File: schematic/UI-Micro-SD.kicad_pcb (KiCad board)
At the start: 2 copper layers, 86.4 x 51.4 mm, 30 parts, among them IC1 TCA9534PWR, J1 47309-3351, J2 Conn_02x04_Odd_Even, J3 Conn_02x05_Odd_Even, J4 Conn_02x03_Odd_Even, J5 Conn_02x08_Odd_Even, J6 Conn_01x08, J7 Conn_02x08_Odd_Even, J8 Solder-Jumper-3-3-3-Open, Q1 BSS138, U1 SFV14R-2STE1HLF, U2 DizzyBITLogo, U3 DizzyBIT-Layout

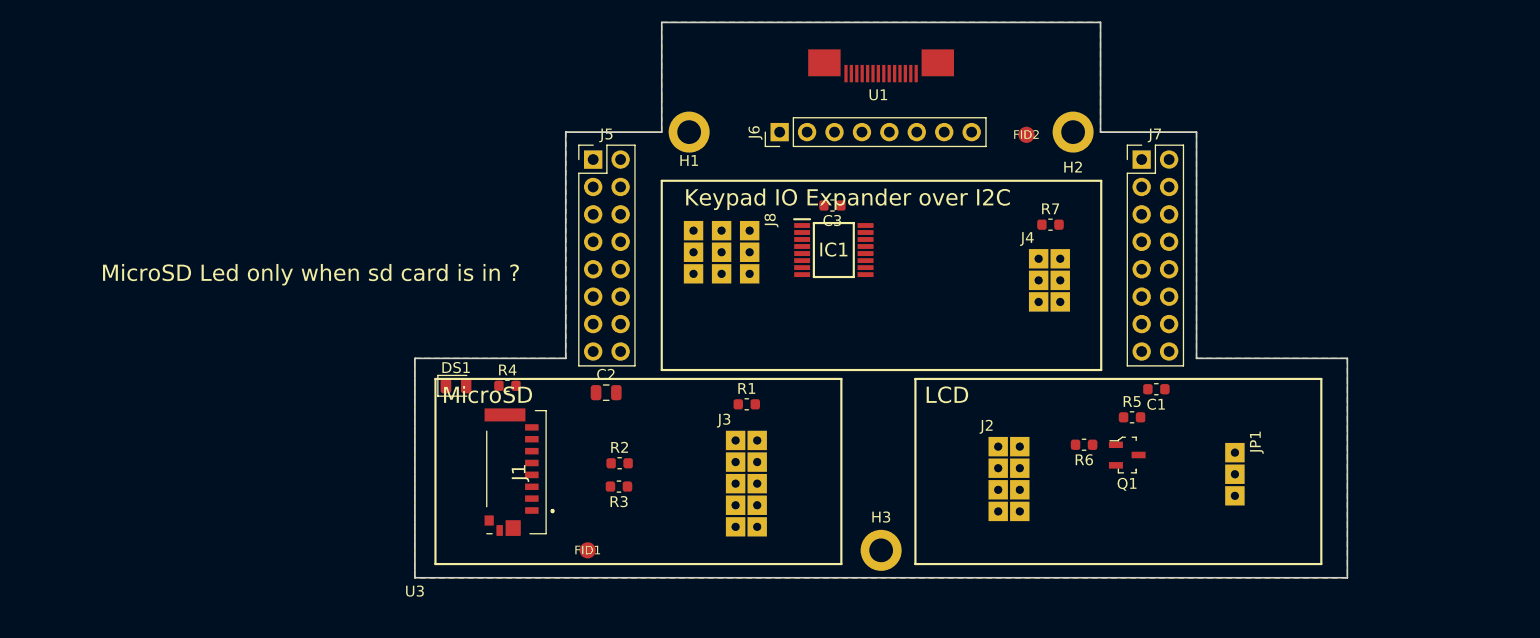
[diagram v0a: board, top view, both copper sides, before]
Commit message: Changed Connector designators
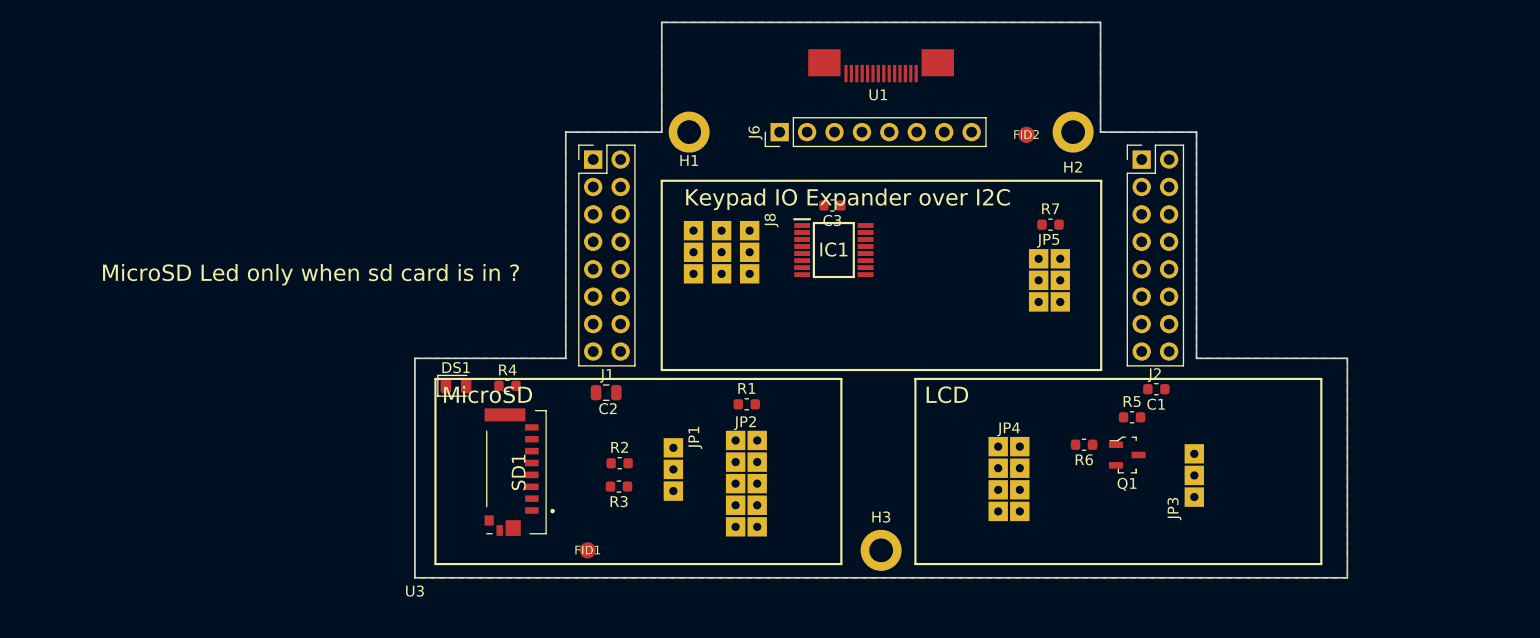
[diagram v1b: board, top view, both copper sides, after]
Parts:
- removed J3: Conn_02x05_Odd_Even, DizzyBit:DizzyBit-SolderJumper-5-5-Open
- removed J4: Conn_02x03_Odd_Even, DizzyBit:DizzyBit-SolderJumper-3-3-Open
- removed J5, J7: Conn_02x08_Odd_Even, Connector_PinHeader_2.54mm:PinHeader_2x08_P2.54mm_Vertical
- added J1: Conn_02x08_Odd_Even, Connector_PinHeader_2.54mm:PinHeader_2x08_P2.54mm_Vertical, F.Cu at (92.7, 107.3)
- added JP2: Conn_02x05_Odd_Even, DizzyBit:DizzyBit-SolderJumper-5-5-Open, F.Cu at (104.9, 132.3)
- added JP3: SolderJumper_3_Bridged12, DizzyBit:DizzyBit-SolderJumper-3-Open, F.Cu at (147.4, 139.6)
- added JP4: Conn_02x04_Odd_Even, DizzyBit:DizzyBit-SolderJumper-4-4-Open, F.Cu at (129.2, 132.9)
- added JP5: Conn_02x03_Odd_Even, DizzyBit:DizzyBit-SolderJumper-3-3-Open, F.Cu at (133.0, 115.5)
- J2: value Conn_02x04_Odd_Even -> Conn_02x08_Odd_Even; footprint DizzyBit:DizzyBit-SolderJumper-4-4-Open -> Connector_PinHeader_2.54mm:PinHeader_2x08_P2.54mm_Vertical
- JP1: value SolderJumper_3_Bridged12 -> SolderJumper_2_Bridged
- moved JP1 52.0 mm to (101.1, 133.0)
- moved J2 29.3 mm to (143.5, 107.3)
- renumbered J1 to SD1
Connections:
- DS1 pad 2: +3V3 -> Net-(DS1-Pad2)
- J2 pad 1: IO17 -> VSPI_MOSI
- J2 pad 2: VSPI_CS -> I2C_SCL
- J2 pad 3: IO16 -> (no net)
- J2 pad 4: VSPI_CS -> (no net)
- J2 pad 5: IO4 -> I2C_SDA
- J2 pad 6: VSPI_CS -> (no net)
- J2 pad 7: IO5 -> VSPI_CLK
- J2 pad 8: VSPI_CS -> IO5
- JP1 pad 2: LCD_BACKLIGHT -> Net-(DS1-Pad2)
- JP1 pad 3: IO2 -> (no net)

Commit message: Working on positioning the components
Changed the MicroSD footprint to match the connfly socket
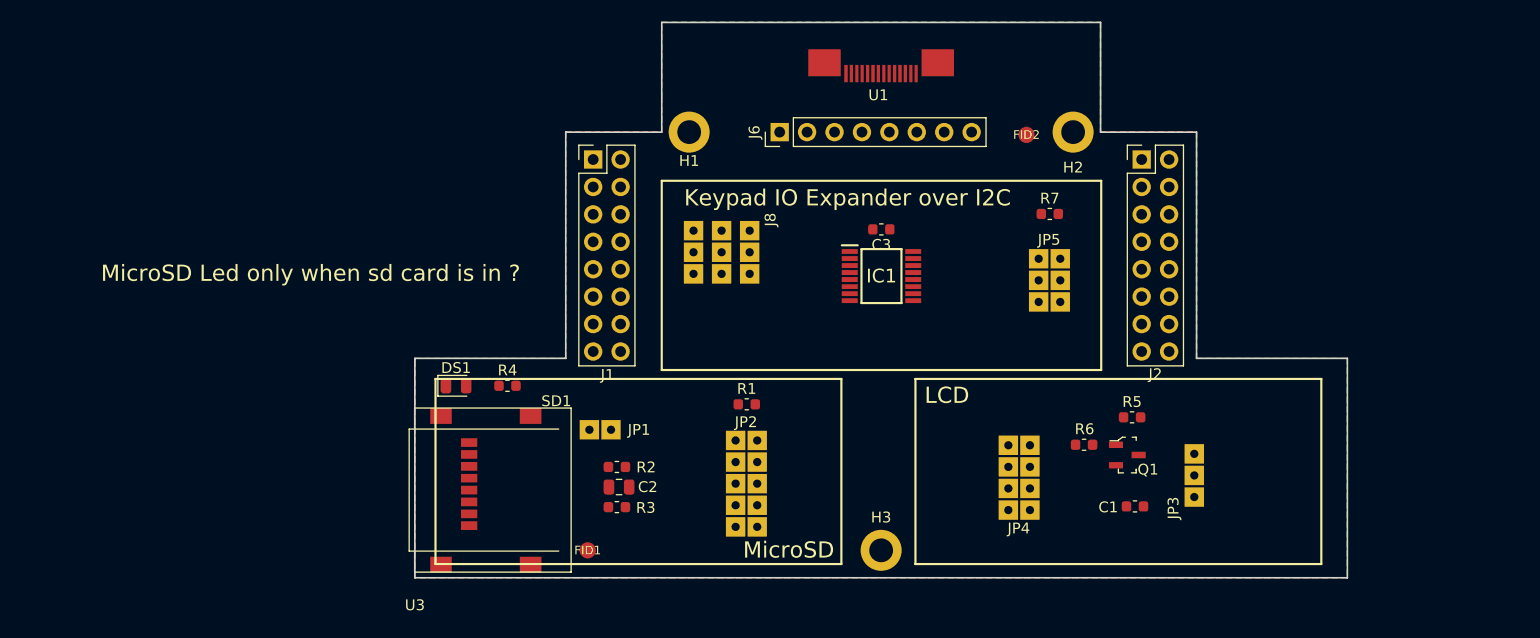
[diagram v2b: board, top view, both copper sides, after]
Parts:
- JP1: footprint DizzyBit:DizzyBit-SolderJumper-3-Open -> DizzyBit:DizzyBit-SolderJumper-2-Open
- SD1: footprint undo:Molex-MicroSD-473093351 -> Connfly:DS-1139-04
- moved C1 11.0 mm to (142.9, 139.4)
- moved JP4 9.30 mm to (134.2, 140.8), turned to 180 degrees
- moved C2 8.82 mm to (95.1, 137.6)
- moved SD1 7.08 mm to (90.7, 131.1)
- moved JP1 5.79 mm to (95.4, 133.3), turned to 180 degrees
- moved C3 5.04 mm to (119.4, 113.8)
- moved IC1 5.03 mm to (119.4, 118.1)
- moved R3 1.91 mm to (94.9, 139.5), turned to 0 degrees
- moved U3 1.27 mm to (76.2, 147.3)
- moved R7 1.00 mm to (135.0, 112.4)
- moved R2 0.43 mm to (94.9, 135.8)
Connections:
- U1 pad MP1: GND -> (no net)
- U1 pad MP2: GND -> (no net)

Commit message: Designed tracks and silk labels
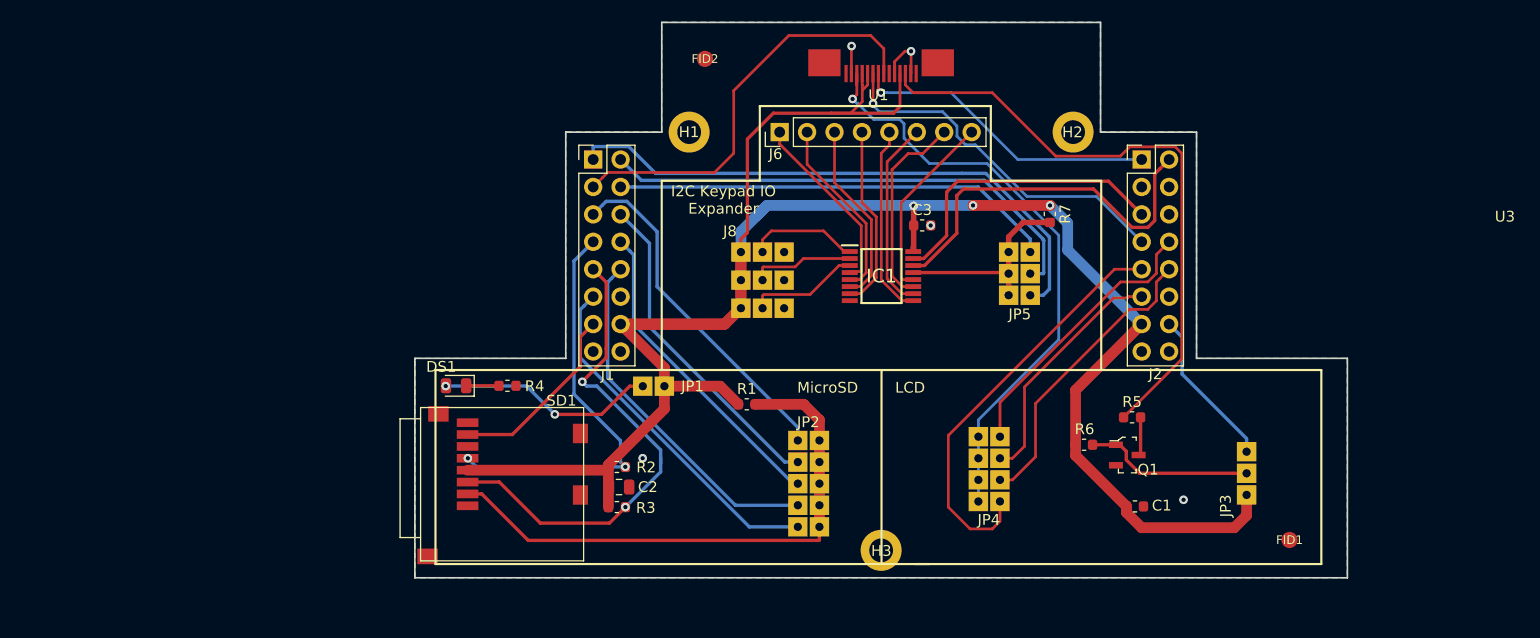
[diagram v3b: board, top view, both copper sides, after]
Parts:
- SD1: footprint Connfly:DS-1139-04 -> Connfly:DS1139-05
- moved U3 107.2 mm to (177.1, 111.3)
- moved FID1 65.0 mm to (157.2, 142.5)
- moved FID2 30.6 mm to (103.1, 98.0)
- moved JP1 6.38 mm to (100.3, 129.3)
- moved JP2 5.76 mm to (110.7, 132.3)
- moved JP5 5.51 mm to (134.2, 120.9), turned to 180 degrees
- moved JP3 4.85 mm to (152.2, 139.4)
- moved C3 3.80 mm to (123.2, 113.4), turned to 0 degrees
- moved J8 3.44 mm to (105.4, 114.9), turned to 0 degrees
- moved JP4 2.89 mm to (131.4, 140.0)
- moved SD1 1.82 mm to (91.5, 132.7)
- moved U2 1.02 mm to (119.1, 116.7)
- turned C1 to 0 degrees
- turned DS1 to 180 degrees
- turned R7 to 270 degrees
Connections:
- J8 pad 2: A0 -> +3V3
- J8 pad 3: GND -> +3V3
- J8 pad 4: +3V3 -> A0
- J8 pad 6: GND -> A2
- J8 pad 7: +3V3 -> GND
- J8 pad 8: A2 -> GND
- JP5 pad 1: I34 -> I39
- JP5 pad 5: I39 -> I34
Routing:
- net +3V3: track 0.00 -> 201.2 mm, vias 0 -> 3
- net LCD_LEDK: track 0.00 -> 56.7 mm
- net VSPI_CS: track 0.00 -> 56.4 mm, vias 0 -> 1
- net I39: track 0.00 -> 53.9 mm
- net HSPI_CS: track 0.00 -> 52.0 mm
- net I36: track 0.00 -> 46.6 mm
- net HSPI_MOSI: track 0.00 -> 45.6 mm, vias 0 -> 2
- net I34: track 0.00 -> 41.1 mm
- net IO17: track 0.00 -> 39.1 mm
- net IO33: track 0.00 -> 38.9 mm
- net HSPI_CLK: track 0.00 -> 38.5 mm, vias 0 -> 2
- net I2C_SCL: track 0.00 -> 35.3 mm
- net VSPI_CLK: track 0.00 -> 33.4 mm, vias 0 -> 1
- net IO27: track 0.00 -> 33.0 mm
- net IO15: track 0.00 -> 32.8 mm
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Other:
- board text added: "+3.3V"
- board text added: "A0"
- board text added: "A1"
- board text added: "A2"
- board text added: "Always ON"
- board text added: "Backlight"
- board text added: "GND"
- board text added: "HSPI CS"
- board text added: "I2C Addr"
- board text added: "I2C Keypad IO Expander"
- board text added: "I34"
- board text added: "I35"
- board text added: "I39"
- board text added: "IO15"
- board text added: "IO16"
- board text added: "IO17"
- board text added: "IO2"
- board text added: "IO25"
- board text added: "IO26"
- board text added: "IO27"
- board text added: "IO32"
- board text added: "IO4"
- board text added: "IO5"
- board text added: "Keypad Interrupt"
- board text added: "Led ON"
- board text added: "VSPI CS"
- board text removed: "Keypad IO Expander over I2C"
- board text removed: "MicroSD Led only when sd card is in ?"
